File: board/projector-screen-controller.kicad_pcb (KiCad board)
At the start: 2 copper layers, 97.2 x 106 mm, 38 parts, among them J1 ICSP, J2 MSTBVA-3-G, J3 RS232 #1, J4 RS232 #2, J5 Buttons, J6 MSTBVA-6-G, K1 JS1-12V-F, K2 JS1-12V-F, K3 JS1-12V-F, K4 JS1-12V-F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

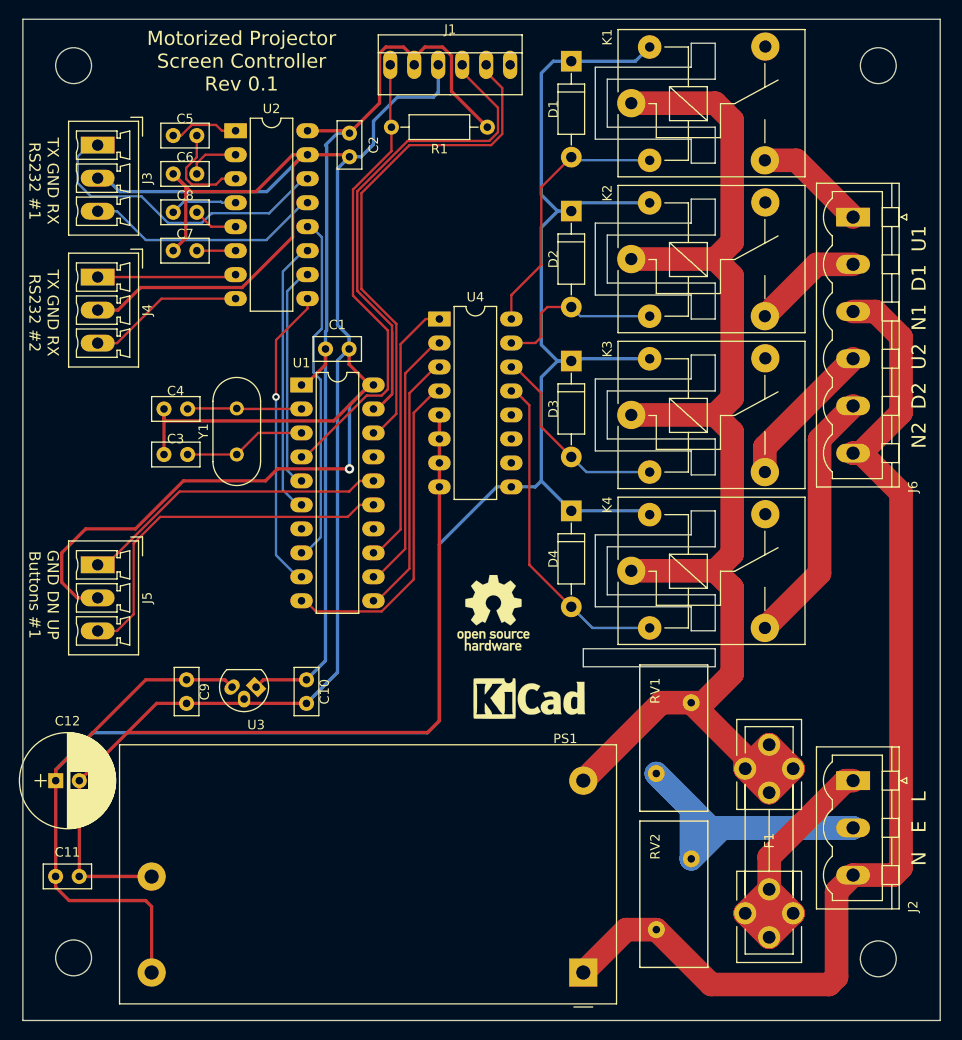
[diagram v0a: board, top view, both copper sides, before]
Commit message: Add button 2, LEDs, TVS diode
* Add button 2; rewire to match the prototype
* Add a TVS diode across the 12V rail; value TBD
* Rework power nets into the power sheet; don't use the globals
  inside the sheet, expose the rails as pins.
* Move power protection inside the power sheet.
* Add power LEDs
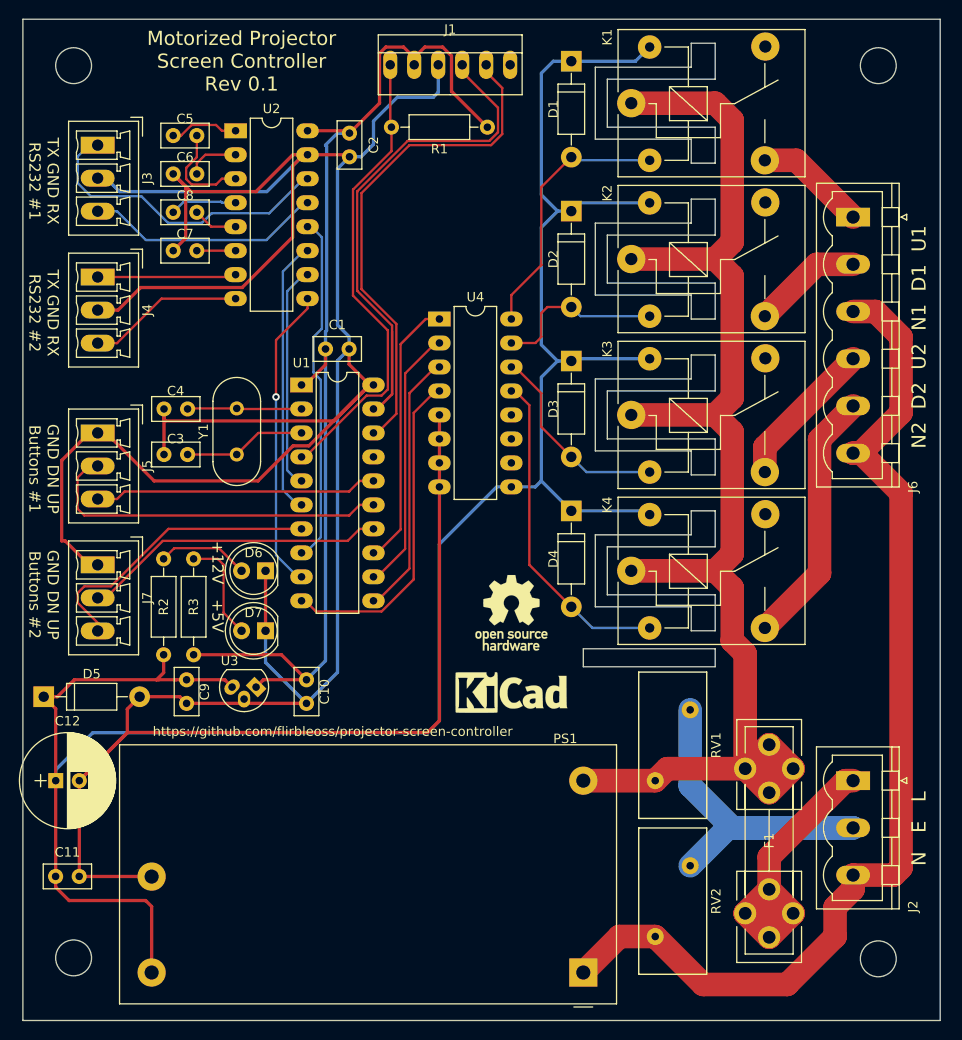
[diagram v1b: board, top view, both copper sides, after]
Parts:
- added D5: D_TVS, Diodes_THT:D_DO-41_SOD81_P10.16mm_Horizontal, F.Cu at (76.8, 116.8)
- added D6: LED, LEDs:LED_D5.0mm, F.Cu at (100.3, 103.5)
- added D7: LED, LEDs:LED_D5.0mm, F.Cu at (100.3, 109.9)
- added J7: MCV-3-G, Connectors_Phoenix:PhoenixContact_MCV-G_03x3.50mm_Vertical, F.Cu at (82.5, 102.9)
- added R2: R, Resistors_THT:R_Axial_DIN0207_L6.3mm_D2.5mm_P10.16mm_Horizontal, F.Cu at (89.5, 112.4)
- added R3: R, Resistors_THT:R_Axial_DIN0207_L6.3mm_D2.5mm_P10.16mm_Horizontal, F.Cu at (92.7, 112.4)
- J3: value RS232 #1 -> MCV-3-G
- J4: value RS232 #2 -> MCV-3-G
- J5: value Buttons -> MCV-3-G
- RV1, RV2: value Varistor -> 360V
- moved J5 14.0 mm to (82.5, 88.9)
- moved RV1 9.09 mm to (141.6, 125.7), turned to 90 degrees
- moved REF** 2.01 mm to (126.4, 116.2)
- moved REF*** 1.91 mm to (126.4, 108.0)
- moved RV2 0.74 mm to (141.6, 142.2)
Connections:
- J1 pad 6: (no net) -> Net-(J1-Pad6)
- J5 pad 1: /MCU/BUTTON_UP -> GND
- J5 pad 2: GND -> /MCU/BUT1_DN
- J5 pad 3: /MCU/BUTTON_DN -> /MCU/BUT1_UP
- K1 pad 4: (no net) -> Net-(K1-Pad4)
- K2 pad 4: (no net) -> Net-(K2-Pad4)
- K3 pad 4: (no net) -> Net-(K3-Pad4)
- K4 pad 4: (no net) -> Net-(K4-Pad4)
- U1 pad 14: (no net) -> /MCU/BUT2_UP
- U1 pad 15: /MCU/BUTTON_DN -> /MCU/BUT1_DN
- U1 pad 16: /MCU/BUTTON_UP -> /MCU/BUT1_UP
- U1 pad 17: (no net) -> Net-(U1-Pad17)
- U1 pad 7: (no net) -> /MCU/BUT2_DN
- U4 pad 10: (no net) -> Net-(U4-Pad10)
- U4 pad 11: (no net) -> Net-(U4-Pad11)
- U4 pad 12: (no net) -> Net-(U4-Pad12)
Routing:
- net /MCU/BUTTON_DN: track 39.1 -> 0.00 mm
- net /MCU/BUT1_DN: track 0.00 -> 38.0 mm
- net /MCU/BUTTON_UP: track 32.9 -> 0.00 mm
- net /MCU/BUT2_DN: track 0.00 -> 32.6 mm
- net /MCU/BUT2_UP: track 0.00 -> 32.2 mm
- net /MCU/BUT1_UP: track 0.00 -> 30.0 mm
- net GND: track 363.8 -> 390.9 mm, vias 1 -> 0
- net +5V: track 104.8 -> 117.8 mm
- net Net-(D7-Pad2): track 0.00 -> 11.2 mm
- net Net-(D6-Pad2): track 0.00 -> 9.71 mm
- net +12V: track 221.2 -> 230.5 mm
- net Earth_Protective: track 52.3 -> 46.0 mm
- net NEUT: track 116.0 -> 112.8 mm
- net LINE: track 150.5 -> 149.0 mm
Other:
- board text added: "+12V +5V"
- board text added: "GND DN UP Buttons #2"
- board text added: "https://github.com/flirbleoss/projector-screen-controller"

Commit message: Update README, add ground planes, adjust clearance
* Update the README with background and a 3d preview image.
* Add ground planes to front and back of logic section; add an earth plane on
  back of line voltage section.
* Check clearances around line voltage input section.
* Change mounting holes to a standard type with plated flange.
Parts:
- added REF**: MountingHole_3.7mm_Pad_Via, Mounting_Holes:MountingHole_3.7mm_Pad_Via, F.Cu at (165.2, 144.6)
- added REF**: MountingHole_3.7mm_Pad_Via, Mounting_Holes:MountingHole_3.7mm_Pad_Via, F.Cu at (165.2, 50.0)
- added REF**: MountingHole_3.7mm_Pad_Via, Mounting_Holes:MountingHole_3.7mm_Pad_Via, F.Cu at (80.0, 50.0)
- added REF**: MountingHole_3.7mm_Pad_Via, Mounting_Holes:MountingHole_3.7mm_Pad_Via, F.Cu at (80.0, 144.5)
- moved F1 2.29 mm to (152.4, 123.8)
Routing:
- net GND: track 390.9 -> 68.1 mm, vias 0 -> 4
- net Earth_Protective: track 46.0 -> 0.00 mm
- net NEUT: track 112.8 -> 106.6 mm
- net /MCU/TX1: track 33.5 -> 29.4 mm
- net Net-(F1-Pad2): track 35.1 -> 37.5 mm
- net /MCU/RX1: track 25.1 -> 23.5 mm
- net Net-(C5-Pad2): track 11.2 -> 10.1 mm
- net +12V: track 230.5 -> 231.4 mm
- added copper zone on B.Cu, net Earth_Protective
- added copper zone on B.Cu, net GND
- added copper zone on F.Cu, net GND
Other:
- outline, holes or cut-outs redrawn

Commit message: Add Solderpad SHL-2.0 license
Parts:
- added REF**: Symbol_HighVoltage_Type2_CopperTop_VerySmall, Symbols:Symbol_HighVoltage_Type2_CopperTop_VerySmall, F.Cu at (160.7, 115.3)
- moved REF** 12.1 mm to (114.3, 116.2)
- moved REF*** 8.84 mm to (117.7, 109.9)
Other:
- board text added: "Copyright (c) Chris Luke Licensed under SHL-2.0"
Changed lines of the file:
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@@
   (general
     (thickness 1.6)
-    (drawings 73)
+    (drawings 74)
     (tracks 335)
     (zones 0)
-    (modules 48)
+    (modules 49)
     (nets 54)
   )
@@
     (title "Projector Screen Controller")
     (rev 0.1)
-    (company "Chris Luke")
+    (company "Flirble Open Source")
     (comment 1 https://github.com/flirbleoss/projector-screen-controller)
+    (comment 2 "Copyright (c) 2019 Chris Luke; licensed under SHL-2.0")
   )
   (layers
@@
     (add_net GND)
   )
+  (module Symbols:Symbol_HighVoltage_Type2_CopperTop_VerySmall (layer F.Cu)
+    (at 160.7185 115.2525)
+    (descr "Symbol, High Voltage, Type 2, Copper Top, Very Small,")
+    (tags "Symbol, High Voltage, Type 2, Copper Top, Very Small,")
+    (fp_text reference REF** (at -0.127 -5.715) (layer F.SilkS) hide
+      (effects (font (size 1 1) (thickness 0.15)))
+    )
+    (fp_text value Symbol_HighVoltage_Type2_CopperTop_VerySmall (at -0.381 4.572) (layer F.Fab) hide
+      (effects (font (size 1 1) (thickness 0.15)))
+    )
+    (fp_line (start -0.49784 2.19964) (end 0.70104 -0.89916) (layer F.Cu) (width 0.381))
+    (fp_line (start 0.70104 -0.89916) (end 0.1016 -0.50038) (layer F.Cu) (width 0.381))
+    (fp_line (start -0.89916 0.20066) (end 0.40132 -2.60096) (layer F.Cu) (width 0.381))
+    (fp_line (start -0.49784 2.19964) (end 0.1016 1.50114) (layer F.Cu) (width 0.381))
+    (fp_line (start -0.09906 -2.79908) (end -0.89916 0.20066) (layer F.Cu) (width 0.381))
+    (fp_line (start -0.89916 0.20066) (end 0.29972 -0.59944) (layer F.Cu) (width 0.381))
+    (fp_line (start 0.29972 -0.59944) (end -0.49784 2.19964) (layer F.Cu) (width 0.381))
+    (fp_line (start -0.49784 2.19964) (end -0.59944 1.30048) (layer F.Cu) (width 0.381))
+    (fp_line (start 0 -4.191) (end 4.699 2.794) (layer F.Cu) (width 0.381))
+    (fp_line (start 4.699 2.794) (end -4.699 2.794) (layer F.Cu) (width 0.381))
+    (fp_line (start -4.699 2.794) (end 0 -4.191) (layer F.Cu) (width 0.381))
+  )
   (module Mounting_Holes:MountingHole_3.7mm_Pad_Via (layer F.Cu)
     (at 165.23 144.6)
@@
   )
   (module Symbols:OSHW-Logo_7.5x8mm_SilkScreen (layer F.Cu)
-    (at 126.365 107.95)
+    (at 117.729 109.855)
     (descr "Open Source Hardware Logo")
     (tags "Logo OSHW")
@@
   )
   (module Symbols:Symbol_KiCAD-Logo_CopperAndSilkScreenTop (layer F.Cu)
-    (at 126.365 116.205)
+    (at 114.3 116.205)
     (descr "Symbol, KiCAD-Logo, Silk & Copper Top,")
     (tags "Symbol, KiCAD-Logo, Silk & Copper Top,")
@@
     )
   )
+  (gr_text "Copyright (c) Chris Luke\nLicensed under SHL-2.0" (at 149.606 148.7805) (layer F.SilkS)
+    (effects (font (size 1 1) (thickness 0.2)))
+  )
   (dimension 106.045 (width 0.12) (layer F.SilkS)

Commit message: Update fuse footprint, add more 3d models, update TODO
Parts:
- C12: footprint Capacitors_THT:CP_Radial_D10.0mm_P2.50mm -> Capacitors_THT:CP_Radial_D10.0mm_P2.50mm_P5.00mm
- D5: value D_TVS -> 15V
- F1: footprint Fuse_Holders_and_Fuses:Fuseholder5x20_horiz_open_universal_Type-III -> Fuse_Holders_and_Fuses:Fuseholder5x20_horiz_open_inline_Type-I
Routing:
- net Net-(F1-Pad2): track 37.5 -> 23.1 mm
- net LINE: track 149.2 -> 135.9 mm
- net GND: track 68.1 -> 70.0 mm
- net +12V: track 231.4 -> 230.0 mm

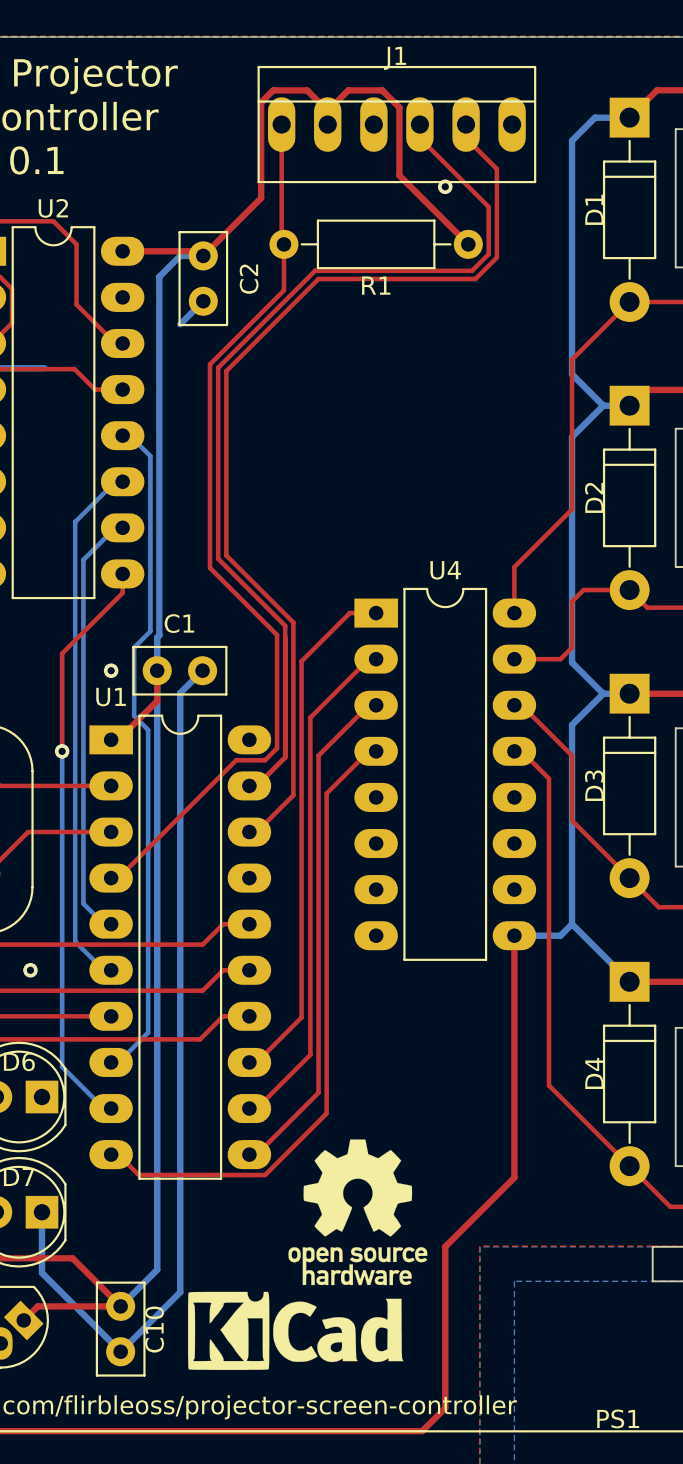
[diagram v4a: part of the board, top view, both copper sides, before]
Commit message: Add relay status LEDs
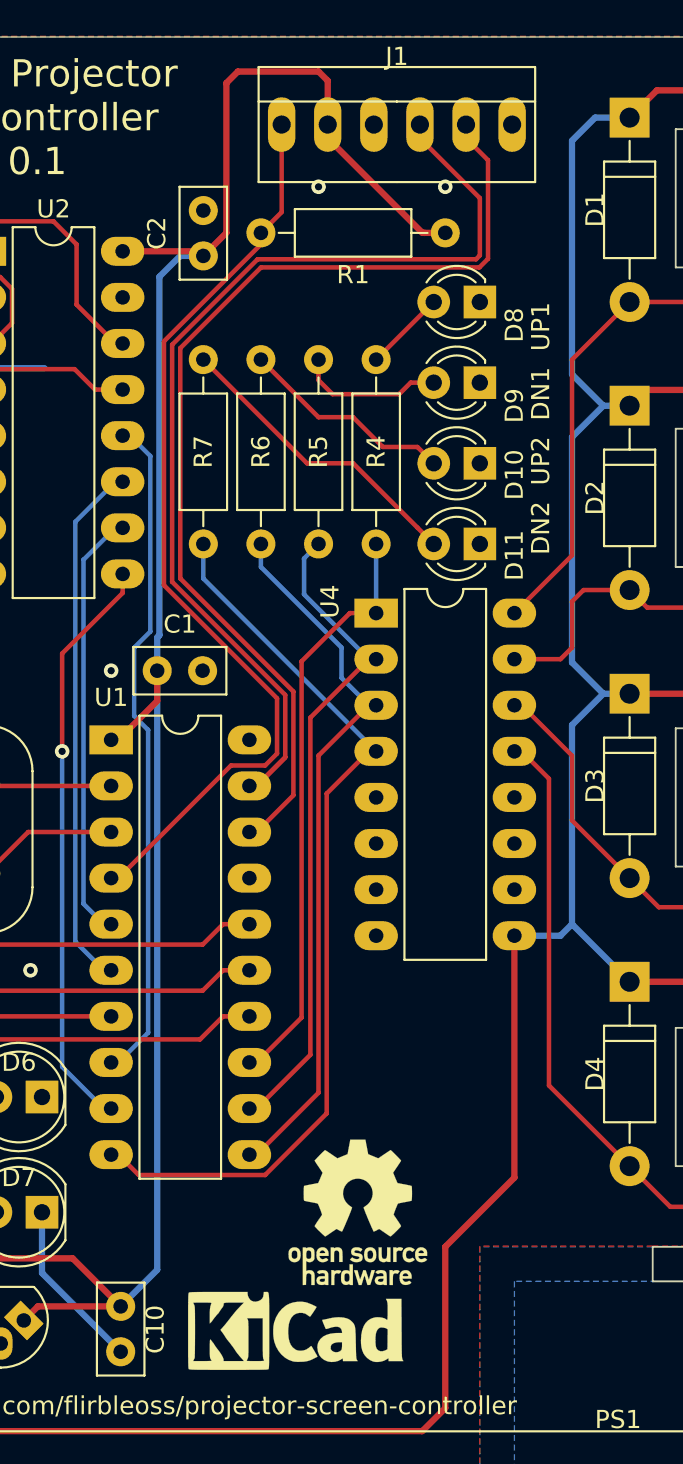
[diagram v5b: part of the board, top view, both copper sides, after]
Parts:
- added D10: LED, LEDs:LED_D3.0mm, F.Cu at (124.5, 68.6)
- added D11: LED, LEDs:LED_D3.0mm, F.Cu at (124.5, 73.0)
- added D8: LED, LEDs:LED_D3.0mm, F.Cu at (124.5, 59.7)
- added D9: LED, LEDs:LED_D3.0mm, F.Cu at (124.5, 64.1)
- added R4: R, Resistors_THT:R_Axial_DIN0207_L6.3mm_D2.5mm_P10.16mm_Horizontal, F.Cu at (118.7, 73.0)
- added R5: R, Resistors_THT:R_Axial_DIN0207_L6.3mm_D2.5mm_P10.16mm_Horizontal, F.Cu at (115.6, 73.0)
- added R6: R, Resistors_THT:R_Axial_DIN0207_L6.3mm_D2.5mm_P10.16mm_Horizontal, F.Cu at (112.4, 73.0)
- added R7: R, Resistors_THT:R_Axial_DIN0207_L6.3mm_D2.5mm_P10.16mm_Horizontal, F.Cu at (109.2, 73.0)
- moved R1 1.42 mm to (122.6, 55.9)
- turned C2 to 90 degrees
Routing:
- net GND: track 70.0 -> 28.8 mm, vias 4 -> 5
- net Net-(D11-Pad2): track 0.00 -> 16.9 mm
- net /MCU/D2_DN_TTL: track 35.1 -> 50.4 mm
- net Net-(D10-Pad2): track 0.00 -> 11.9 mm
- net /MCU/D2_UP_TTL: track 28.1 -> 39.9 mm
- net /MCU/D1_DN_TTL: track 28.5 -> 37.1 mm
- net Net-(D9-Pad2): track 0.00 -> 8.06 mm
- net Net-(D8-Pad2): track 0.00 -> 4.49 mm
- net /MCU/D1_UP_TTL: track 28.7 -> 32.6 mm
- net Net-(J1-Pad5): track 53.7 -> 57.4 mm
- net Net-(J1-Pad4): track 60.7 -> 57.8 mm
- net Net-(J1-Pad1): track 49.8 -> 51.9 mm
- net +5V: track 117.7 -> 116.8 mm
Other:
- board text added: "DN2 UP2 DN1 UP1"

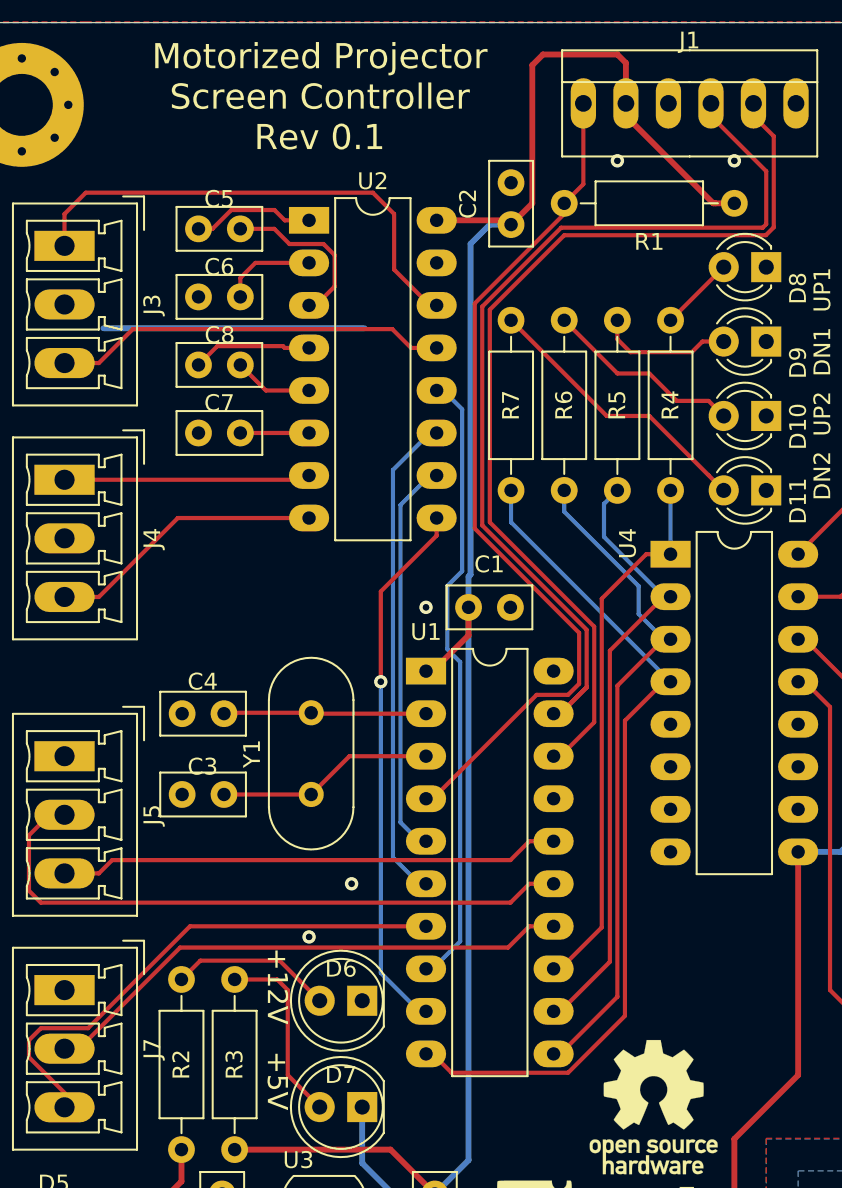
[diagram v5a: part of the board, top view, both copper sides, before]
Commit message: Add nominal LED R values; ground plane tweaks; first board spin
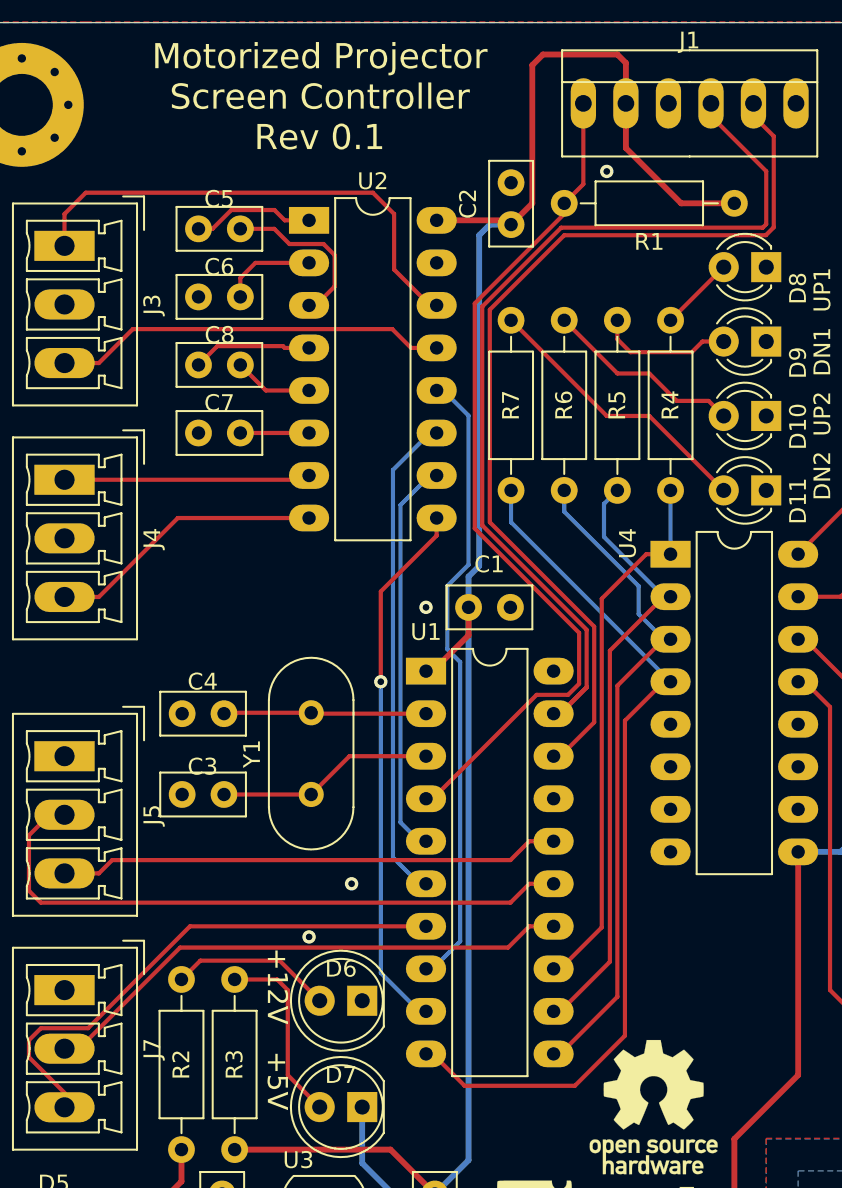
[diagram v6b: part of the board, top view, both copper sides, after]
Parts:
- R2: value R -> 500R
- R3, R4, R5, R6, R7: value R -> 150R
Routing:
- net GND: track 28.8 -> 13.2 mm, vias 5 -> 4
- net /MCU/D2_DN_TTL: track 50.4 -> 51.8 mm
- net +5V: track 116.8 -> 117.9 mm
